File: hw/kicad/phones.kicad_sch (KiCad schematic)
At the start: 20 parts, among them J801 НАУШН./ЛИН., U801 TPA6132A2

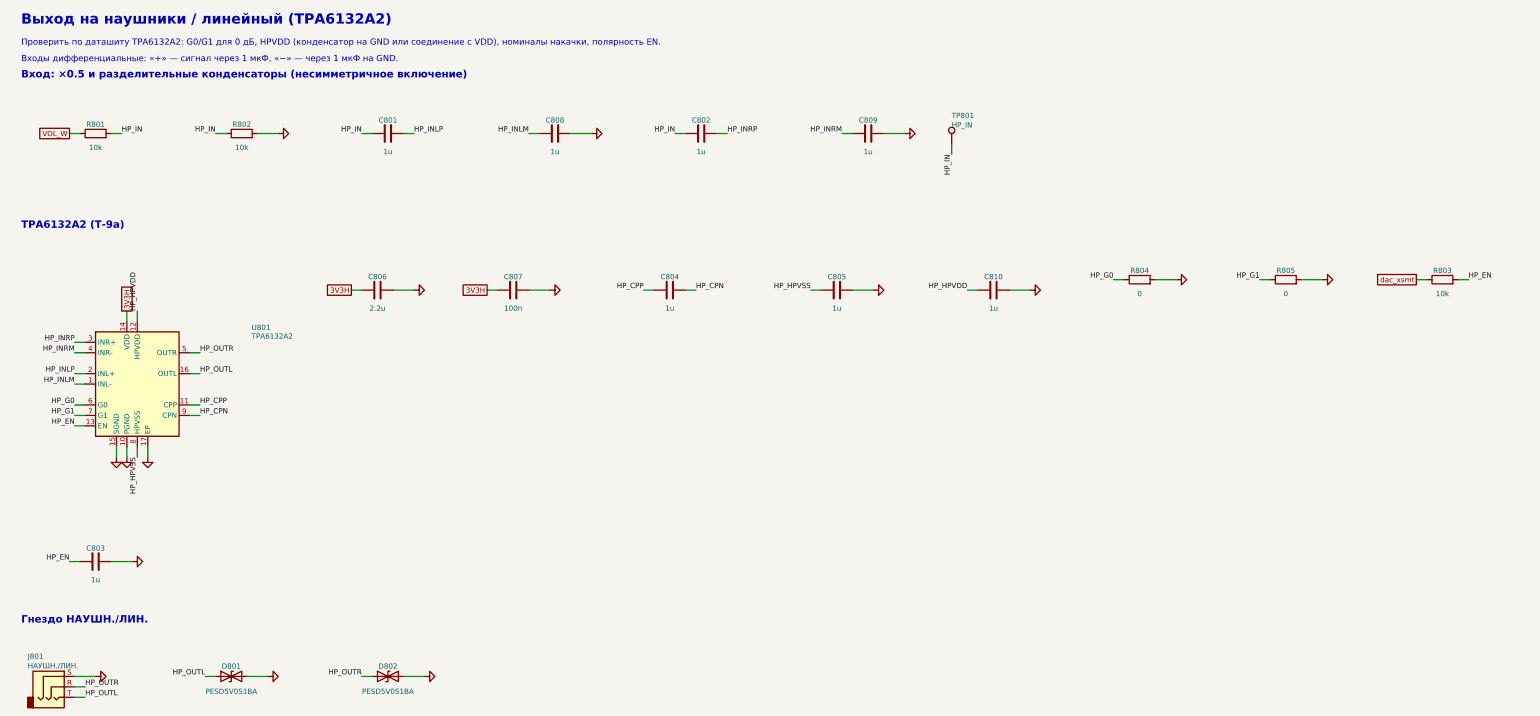
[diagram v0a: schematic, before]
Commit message: Reorganize KiCad schematic into 7 functional sheets with framed blocks
- Sheets: power, fpga, midi_sync, analog_in (inputs + ADC), audio_out
  (DAC + OUT/OUT2 + clip LEDs), phones, panel
- Each functional block is drawn in a dashed frame with a title; blocks are
  tiled across the sheet, A3/A2 chosen automatically
- Netlist check still 153/153; PDF and docs updated

Co-Authored-By: Claude Opus 5.5 <noreply@anthropic.com>
Claude-Session: https://claude.ai/code/session_01JcNV2ZCXWxtNzRVWffkrjk
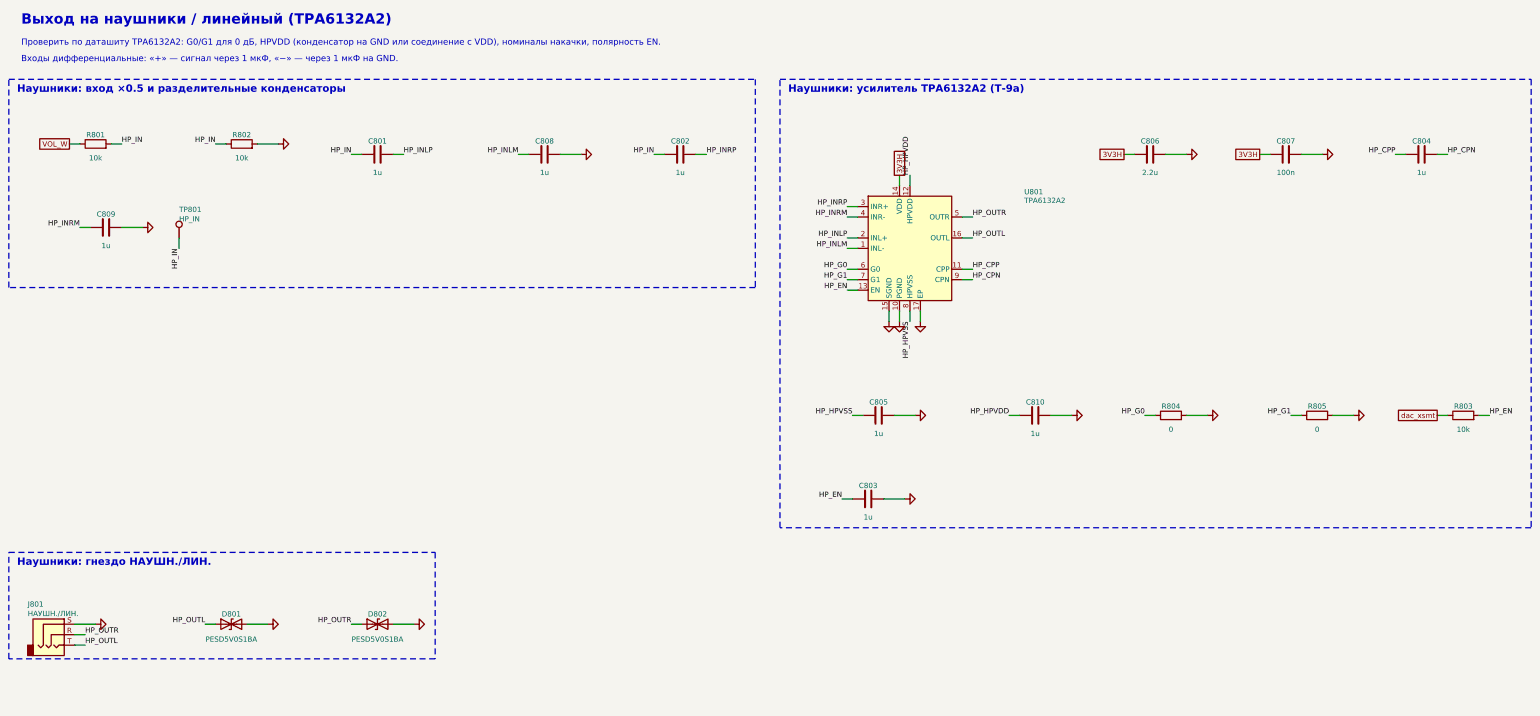
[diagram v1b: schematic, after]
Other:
- note added: "Наушники: вход ×0.5 и разделительные конденсаторы"
- note added: "Наушники: гнездо НАУШН./ЛИН."
- note added: "Наушники: усилитель TPA6132A2 (Т-9a)"
- note removed: "TPA6132A2 (Т-9a)"
- note removed: "Вход: ×0.5 и разделительные конденсаторы (несимметричное включение)"
- note removed: "Гнездо НАУШН./ЛИН."
- moved on the sheet: C801, C802, C803, C804, C805, C806, C807, C808, C809, C810, D801, D802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
